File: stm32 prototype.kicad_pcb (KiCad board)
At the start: 4 copper layers, 133 parts, among them J1 USB_B_Mini, J2 Conn_01x06, J3 Conn_01x02, J4 Conn_01x10, Q1 Q_NMOS_GSD, Q2 Q_NMOS_GSD, Q3 Q_NMOS_GSD, Q4 Q_NMOS_GSD, Q5 Q_NMOS_GSD, Q6 Q_NMOS_GSD, Q7 Q_NMOS_GSD, Q8 Q_NMOS_GSD, Q9 Q_NMOS_GSD, U1 FT232RL, U2 W25Q128JV-DTR, U3 STM32F407VGTx, U4 LD1117S33TR, U5 ESP32, U6 IS25LP016D-JNLE-TR, U7 TPS62203DBVR, Y1 Crystal_GND24, Y2 Crystal_GND23, Y3 Crystal_GND23

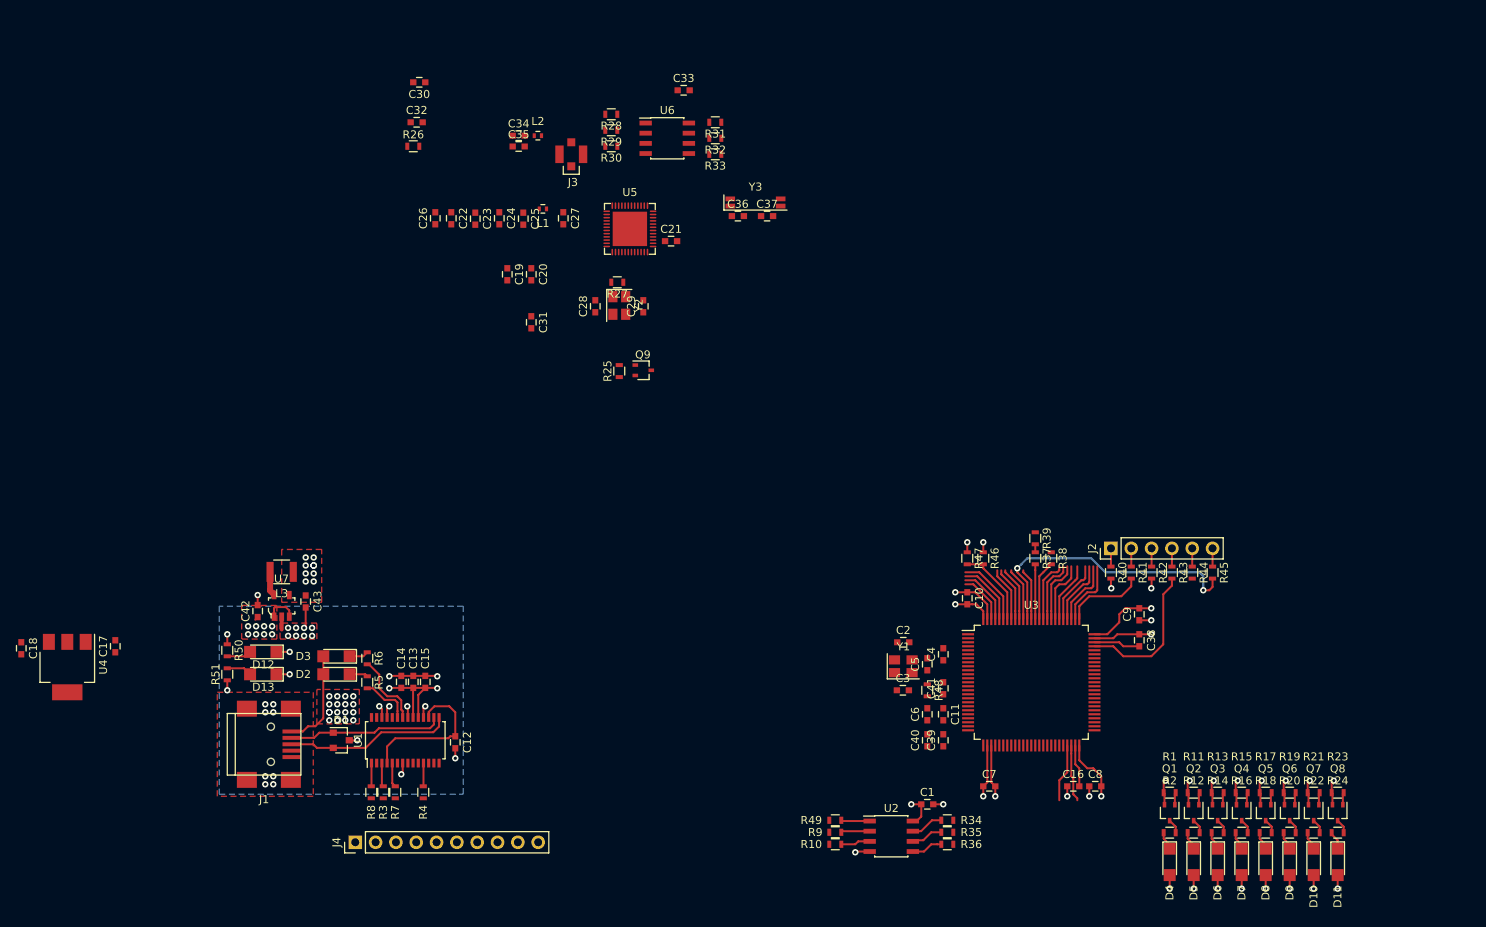
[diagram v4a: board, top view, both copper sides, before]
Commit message: laid out reserve linear 3.3V regulator, wired up FTDI header
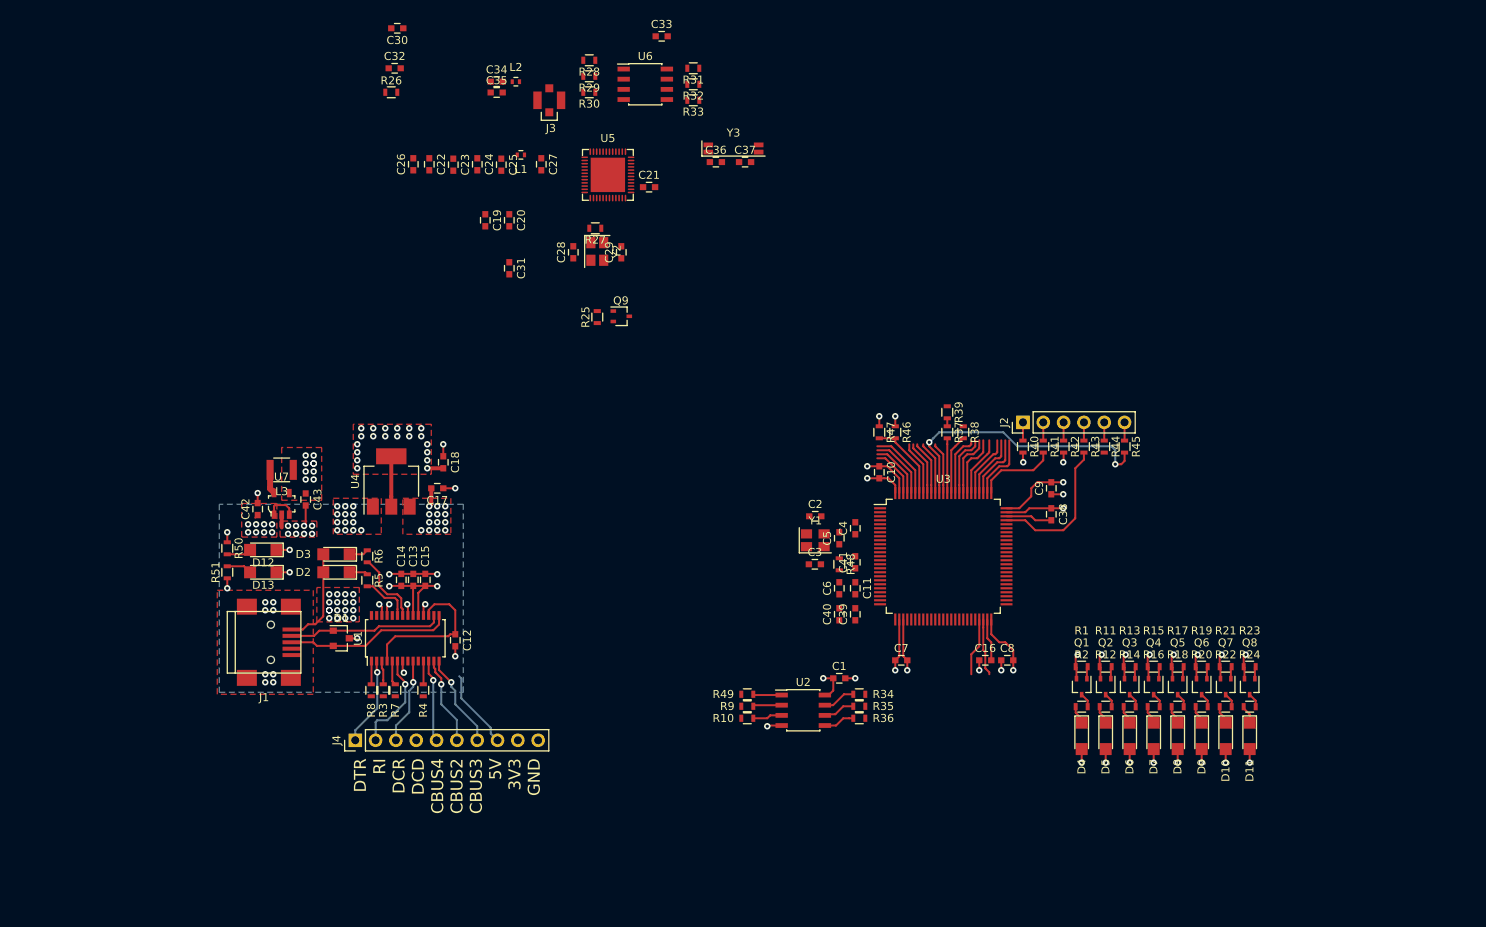
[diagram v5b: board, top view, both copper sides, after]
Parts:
- C17: value C -> 0.1uF
- C18: value C -> 10uF
- moved C18 57.6 mm to (97.0, 103.5)
- moved U4 46.7 mm to (90.5, 105.9), turned to 90 degrees
- moved C17 44.8 mm to (96.2, 106.8), turned to 180 degrees
- moved C1 19.2 mm to (146.5, 130.5)
- moved C10 19.2 mm to (151.5, 104.8)
- moved C11 19.2 mm to (148.5, 119.2)
- moved C16 19.2 mm to (164.8, 128.2)
- moved C2 19.2 mm to (143.5, 110.2)
- moved C3 19.2 mm to (143.4, 116.2)
- moved C38 19.2 mm to (173.0, 110.0)
- moved C39 19.2 mm to (148.5, 122.5)
- moved C4 19.2 mm to (148.5, 111.8)
- moved C40 19.2 mm to (146.5, 122.5)
- moved C41 19.2 mm to (148.5, 116.0)
- moved C5 19.2 mm to (146.5, 113.0)
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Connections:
- U4 pad 4: (no net) -> +3V3
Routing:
- net FTDI_RI: track 0.00 -> 12.6 mm, vias 0 -> 1
- net +5V: track 31.9 -> 44.2 mm, vias 29 -> 42
- net FTDI_CBUS3: track 0.00 -> 11.9 mm, vias 0 -> 1
- net FTDI_CBUS2: track 0.00 -> 11.1 mm, vias 0 -> 1
- net FTDI_DTR: track 0.00 -> 11.1 mm, vias 0 -> 1
- net FTDI_DCR: track 0.00 -> 10.8 mm, vias 0 -> 1
- net FTDI_CBUS4: track 0.00 -> 10.3 mm, vias 0 -> 1
- net +3V3: track 49.8 -> 58.1 mm, vias 26 -> 46
- net GND: track 79.6 -> 82.6 mm, vias 46 -> 61
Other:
- board text added: "DTR RI DCR DCD CBUS4 CBUS2 CBUS3 5V 3V3 GND"

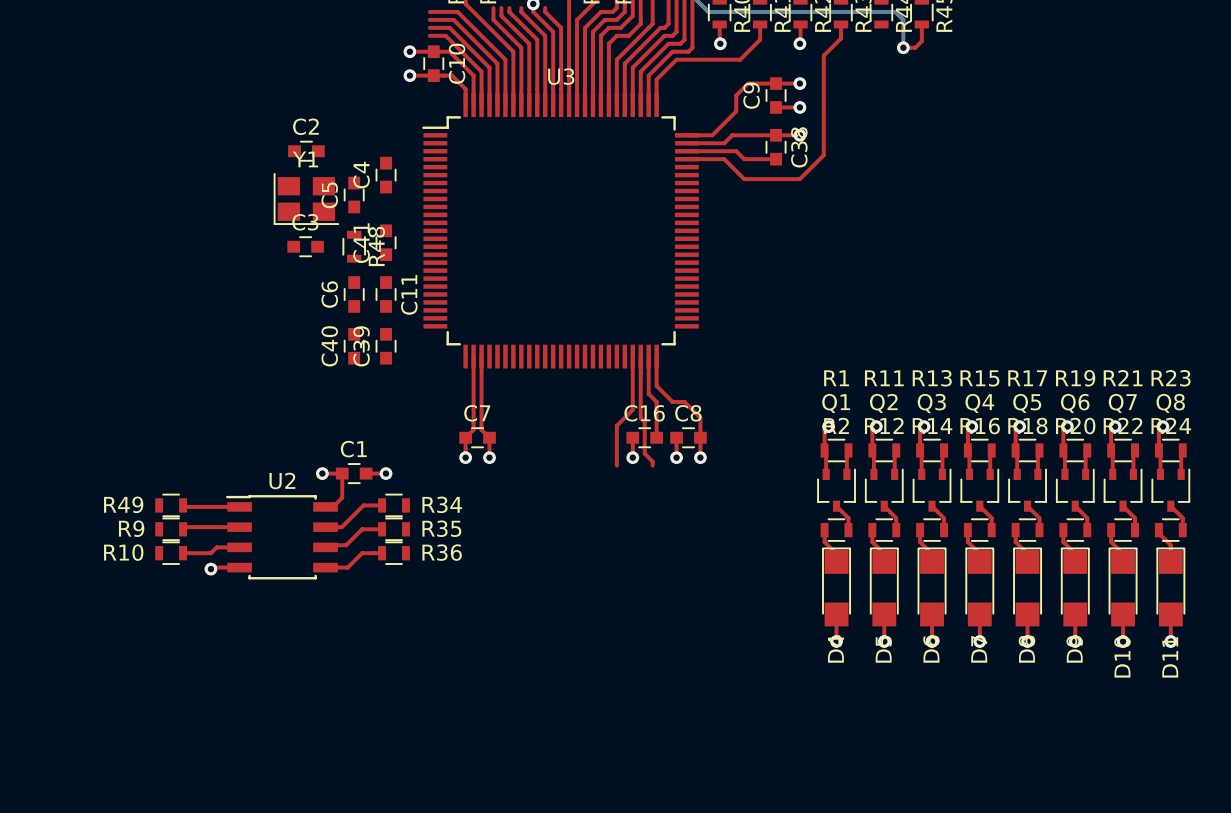
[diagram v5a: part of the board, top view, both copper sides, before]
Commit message: laid out crystal oscilator, connected binary indicator leds
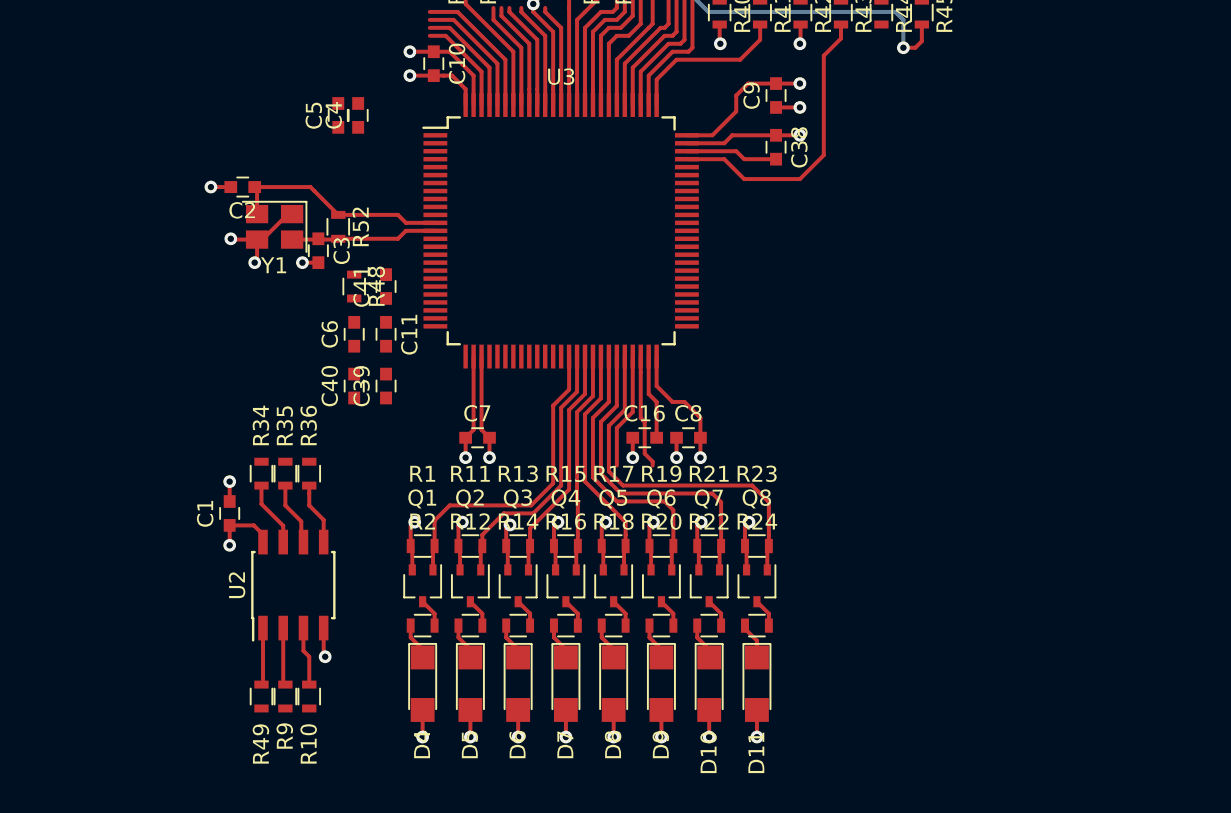
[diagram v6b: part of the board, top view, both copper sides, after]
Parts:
- added R52: 1MR, Resistors_SMD:R_0603, F.Cu at (145.5, 115.0)
- moved D10 26.7 mm to (168.8, 143.7)
- moved D11 26.7 mm to (171.8, 143.7)
- moved D4 26.7 mm to (150.8, 143.7)
- moved D5 26.7 mm to (153.8, 143.7)
- moved D6 26.7 mm to (156.8, 143.7)
- moved D7 26.7 mm to (159.8, 143.7)
- moved D8 26.7 mm to (162.8, 143.7)
- moved D9 26.7 mm to (165.8, 143.7)
- moved Q1 26.7 mm to (150.8, 137.6)
- moved Q2 26.7 mm to (153.8, 137.6)
- moved Q3 26.7 mm to (156.8, 137.6)
- moved Q4 26.7 mm to (159.8, 137.6)
- moved Q5 26.7 mm to (162.8, 137.6)
- moved Q6 26.7 mm to (165.8, 137.6)
- moved Q7 26.7 mm to (168.8, 137.6)
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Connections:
- U3 pad 39: STATUS_BIT7 -> STATUS_BIT0
- U3 pad 40: STATUS_BIT6 -> STATUS_BIT1
- U3 pad 41: STATUS_BIT5 -> STATUS_BIT2
- U3 pad 42: STATUS_BIT4 -> STATUS_BIT3
- U3 pad 43: STATUS_BIT3 -> STATUS_BIT4
- U3 pad 44: STATUS_BIT2 -> STATUS_BIT5
- U3 pad 45: STATUS_BIT1 -> STATUS_BIT6
- U3 pad 46: STATUS_BIT0 -> STATUS_BIT7
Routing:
- net STATUS_BIT7: track 1.54 -> 22.8 mm
- net STATUS_BIT6: track 1.54 -> 20.4 mm
- net STATUS_BIT0: track 1.54 -> 19.9 mm
- net STATUS_BIT5: track 1.54 -> 17.7 mm
- net STATUS_BIT1: track 1.54 -> 17.0 mm
- net Net-(C2-Pad1): track 0.00 -> 14.0 mm
- net STATUS_BIT4: track 1.54 -> 14.9 mm
- net STATUS_BIT2: track 1.54 -> 14.9 mm
- net STATUS_BIT3: track 1.54 -> 13.9 mm
- net Net-(C3-Pad1): track 0.00 -> 9.23 mm
- net GND: track 82.6 -> 90.7 mm, vias 61 -> 65

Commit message: worked on stm flash chip layout, stm bypass capacitor layout, changed antenna connection to sma
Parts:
- J3: footprint connectors_mdg:u.FL -> connectors_mdg:SMA_SMD_Jack_Straight
- moved R45 68.6 mm to (122.8, 136.0), turned to 90 degrees
- moved R44 64.2 mm to (125.4, 136.0), turned to 90 degrees
- moved D11 63.1 mm to (133.2, 93.8), turned to 90 degrees
- moved R43 60.0 mm to (127.9, 136.0), turned to 90 degrees
- moved D10 59.6 mm to (136.2, 93.8), turned to 90 degrees
- moved R49 58.0 mm to (167.1, 92.8), turned to 270 degrees
- moved R24 57.5 mm to (133.2, 97.5), turned to 180 degrees
- moved R9 56.7 mm to (165.6, 92.8), turned to 270 degrees
- moved D9 56.5 mm to (139.2, 93.8), turned to 90 degrees
- moved R42 55.9 mm to (130.5, 136.0), turned to 90 degrees
- moved R10 55.5 mm to (164.1, 92.8), turned to 270 degrees
- moved D8 54.0 mm to (142.2, 93.8), turned to 90 degrees
- moved Q8 53.9 mm to (133.2, 100.0), turned to 90 degrees
- moved R22 53.6 mm to (136.2, 97.5), turned to 180 degrees
- moved J2 52.8 mm to (135.5, 139.0), turned to 270 degrees
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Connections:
- U3 pad 18: (no net) -> ST_HOLD
- U3 pad 67: ST_HOLD -> (no net)
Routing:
- net (no net): track 149.8 -> 235.6 mm, vias 0 -> 8
- net +3V3: track 58.1 -> 116.0 mm, vias 46 -> 52
- net MEM_CHIP_SELECT: track 0.00 -> 46.3 mm, vias 0 -> 2
- net NRST: track 0.00 -> 45.8 mm, vias 0 -> 2
- net ST_MISO: track 0.00 -> 40.4 mm, vias 0 -> 2
- net ST_WP: track 0.00 -> 31.4 mm, vias 0 -> 2
- net ST_SCK: track 0.00 -> 25.9 mm
- net ST_MOSI: track 0.00 -> 25.3 mm
- net ST_HOLD: track 0.00 -> 22.8 mm
- net GND: track 90.7 -> 110.0 mm, vias 65 -> 73
- net /ESP32_VOLTAGE_SENSE: track 0.00 -> 13.0 mm
- net Net-(R9-Pad2): track 3.61 -> 2.86 mm
- net Net-(R49-Pad2): track 3.59 -> 2.84 mm
- net Net-(R10-Pad2): track 3.70 -> 2.95 mm

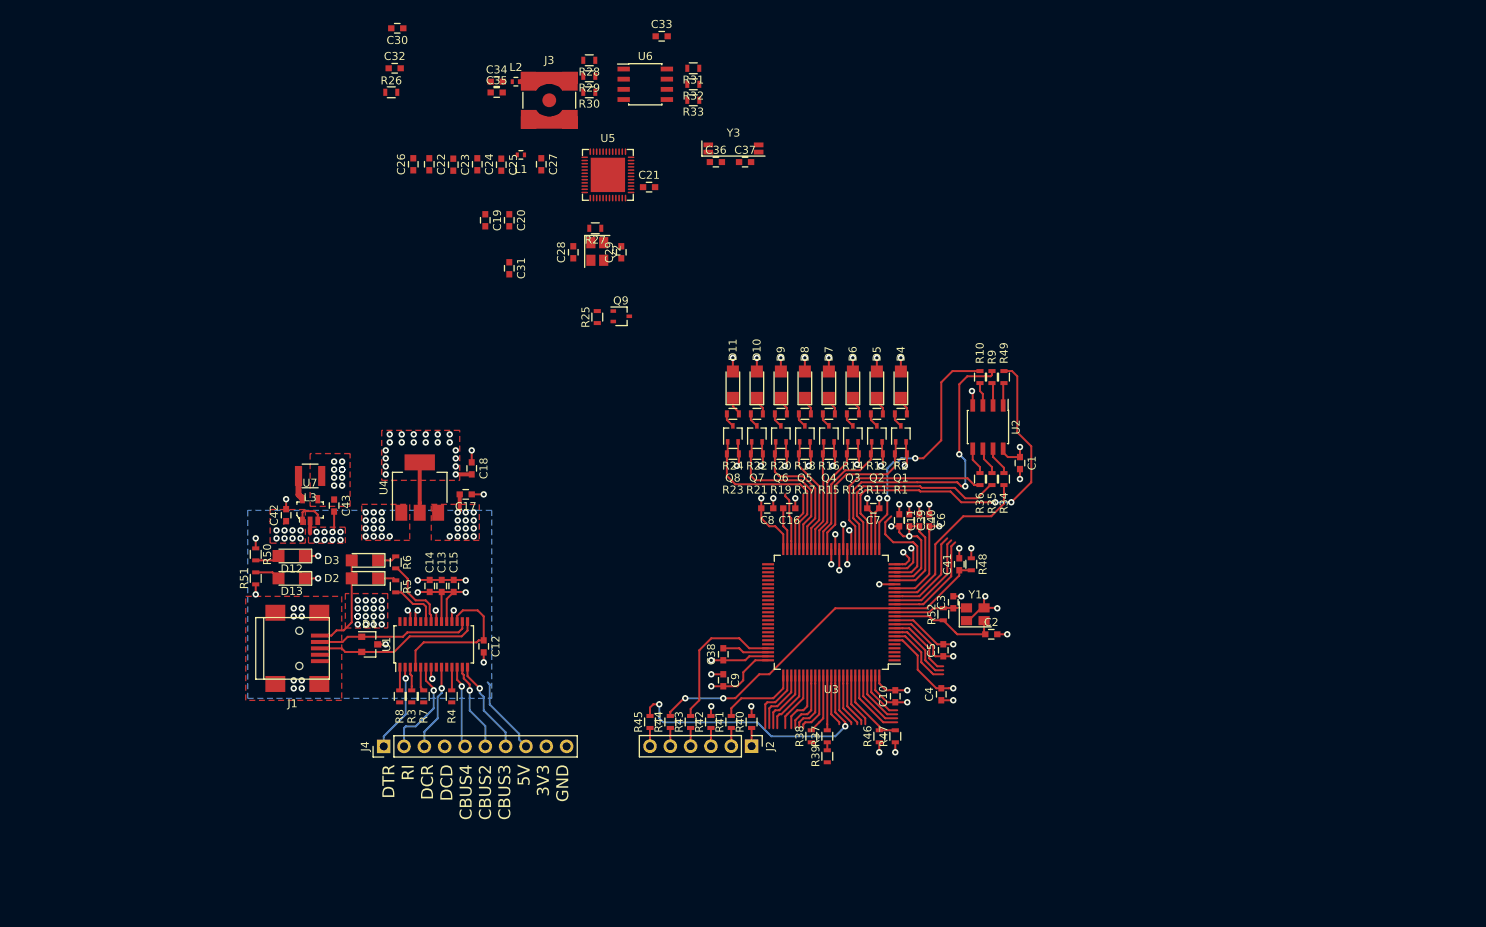
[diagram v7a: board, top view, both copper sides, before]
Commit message: did a little layout around esp32, need to check pinout of stm crystal, need to check trace width and spacing for esp32
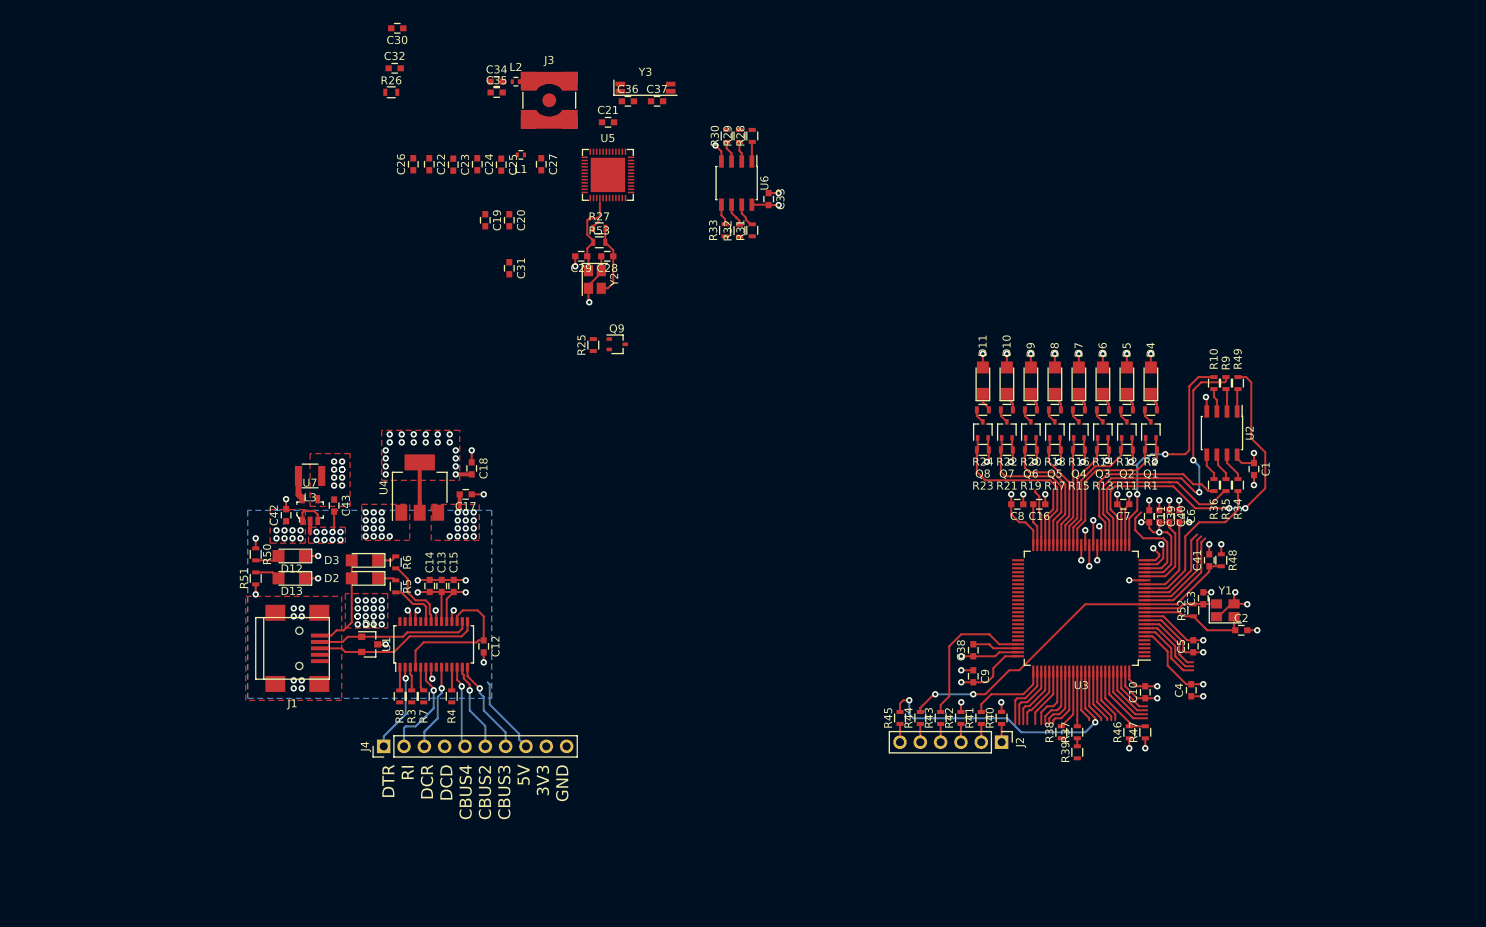
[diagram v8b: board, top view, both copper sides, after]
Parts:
- added R53: 1MR, Resistors_SMD:R_0603, F.Cu at (116.5, 76.0)
- Y2: value Crystal_GND23 -> Crystal_GND24
- moved C10 31.3 mm to (184.8, 132.2)
- moved C11 31.3 mm to (185.2, 110.2)
- moved C16 31.3 mm to (171.5, 108.8)
- moved C2 31.3 mm to (196.8, 124.5)
- moved C3 31.3 mm to (192.0, 120.5)
- moved C38 31.3 mm to (163.2, 127.0)
- moved C39 31.3 mm to (186.5, 110.2)
- moved C4 31.3 mm to (190.5, 132.0)
- moved C40 31.3 mm to (187.8, 110.2)
- moved C41 31.3 mm to (192.8, 115.8)
- moved C5 31.3 mm to (190.8, 126.5)
- moved C6 31.3 mm to (189.0, 110.2)
- moved C7 31.3 mm to (182.0, 108.8)
- moved C8 31.3 mm to (168.8, 108.8)
- moved C9 31.3 mm to (163.2, 130.2)
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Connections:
- Y2 pad 1: Net-(C28-Pad1) -> Net-(C29-Pad1)
- Y2 pad 3: GND -> Net-(C28-Pad1)
- Y2 pad 4: Net-(C29-Pad1) -> GND
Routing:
- net GND: track 110.0 -> 121.2 mm, vias 73 -> 77
- net Net-(C29-Pad1): track 0.00 -> 10.5 mm
- net Net-(C28-Pad1): track 0.00 -> 9.02 mm
- net +3V3: track 116.0 -> 119.3 mm, vias 52 -> 53
- net Net-(R31-Pad2): track 0.00 -> 3.11 mm
- net Net-(R32-Pad2): track 0.00 -> 2.91 mm
- net Net-(R30-Pad1): track 0.00 -> 2.70 mm
- net Net-(R33-Pad2): track 0.00 -> 2.64 mm
- net Net-(R29-Pad1): track 0.00 -> 2.57 mm
- net Net-(R28-Pad1): track 0.00 -> 2.47 mm
- net ST_HOLD: track 22.8 -> 20.6 mm
- net ST_WP: track 31.4 -> 29.3 mm
- net MEM_CHIP_SELECT: track 46.3 -> 44.8 mm
- net ST_MOSI: track 25.3 -> 23.8 mm
- net ST_MISO: track 40.4 -> 38.9 mm
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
